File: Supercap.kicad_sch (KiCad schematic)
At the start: 0 parts

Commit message: began setup of hierarchial boards for supercap
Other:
- added sheet Control (Control/control.kicad_sch)
- added sheet Housekeeping (Housekeeping/housekeeping.kicad_sch)
- added sheet Supercap (Supercap/supercap.kicad_sch)
- added sheet Voltage Converter (Converter/converter.kicad_sch)
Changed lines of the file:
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@@
 	(generator_version "9.0")
 	(paper "A4")
+	(sheet
+		(at 109.22 68.58)
+		(size 41.91 25.4)
+		(exclude_from_sim no)
+		(in_bom yes)
+		(on_board yes)
+		(dnp no)
+		(fields_autoplaced yes)
+		(stroke
+			(width 0.1524)
+			(type solid)
+		)
+		(fill
+			(color 0 0 0 0.0000)
+		)
+		(property "Sheetname" "Housekeeping"
+			(at 109.22 67.8684 0)
+			(effects
+				(font
+					(size 1.27 1.27)
+				)
+				(justify left bottom)
+			)
+		)
+		(property "Sheetfile" "Housekeeping/housekeeping.kicad_sch"
+			(at 109.22 94.5646 0)
+			(effects
+				(font
+					(size 1.27 1.27)
+				)
+				(justify left top)
+			)
+		)
+		(instances
+			(project "Supercap"
+				(path "/98ee8313-37ab-4329-91ab-b5710476f82f"
+					(page "3")
+				)
+			)
+		)
+	)
+	(sheet
+		(at 158.75 68.58)
+		(size 39.37 25.4)
+		(exclude_from_sim no)
+		(in_bom yes)
+		(on_board yes)
+		(dnp no)
+		(fields_autoplaced yes)
+		(stroke
+			(width 0.1524)
+			(type solid)
+		)
+		(fill
+			(color 0 0 0 0.0000)
+		)
+		(property "Sheetname" "Voltage Converter"
+			(at 158.75 67.8684 0)
+			(effects
+				(font
+					(size 1.27 1.27)
+				)
+				(justify left bottom)
+			)
+		)
+		(property "Sheetfile" "Converter/converter.kicad_sch"
+			(at 158.75 94.5646 0)
+			(effects
+				(font
+					(size 1.27 1.27)
+				)
+				(justify left top)
+			)
+		)
+		(instances
+			(project "Supercap"
+				(path "/98ee8313-37ab-4329-91ab-b5710476f82f"
+					(page "4")
+				)
+			)
+		)
+	)
+	(sheet
+		(at 208.28 68.58)
+		(size 40.64 25.4)
+		(exclude_from_sim no)
+		(in_bom yes)
+		(on_board yes)
+		(dnp no)
+		(fields_autoplaced yes)
+		(stroke
+			(width 0.1524)
+			(type solid)
+		)
+		(fill
+			(color 0 0 0 0.0000)
+		)
+		(property "Sheetname" "Supercap"
+			(at 208.28 67.8684 0)
+			(effects
+				(font
+					(size 1.27 1.27)
+				)
+				(justify left bottom)
+			)
+		)
+		(property "Sheetfile" "Supercap/supercap.kicad_sch"
+			(at 208.28 94.5646 0)
+			(effects
+				(font
+					(size 1.27 1.27)
+				)
+				(justify left top)
+			)
+		)
+		(instances
+			(project "Supercap"
+				(path "/98ee8313-37ab-4329-91ab-b5710476f82f"
+					(page "5")
+				)
+			)
+		)
+	)
+	(sheet
+		(at 54.61 67.31)
+		(size 44.45 26.67)
+		(exclude_from_sim no)
+		(in_bom yes)
+		(on_board yes)
+		(dnp no)
+		(fields_autoplaced yes)
+		(stroke
+			(width 0.1524)
+			(type solid)
+		)
+		(fill
+			(color 0 0 0 0.0000)
+		)
+		(property "Sheetname" "Control"
+			(at 54.61 66.5984 0)
+			(effects
+				(font
+					(size 1.27 1.27)
+				)
+				(justify left bottom)
+			)
+		)
+		(property "Sheetfile" "Control/control.kicad_sch"
+			(at 54.61 94.5646 0)
+			(effects
+				(font
+					(size 1.27 1.27)
+				)
+				(justify left top)
+			)
+		)
+		(instances
+			(project "Supercap"
+				(path "/98ee8313-37ab-4329-91ab-b5710476f82f"
+					(page "2")
+				)
+			)
+		)
+	)
 	(sheet_instances
 		(path "/"

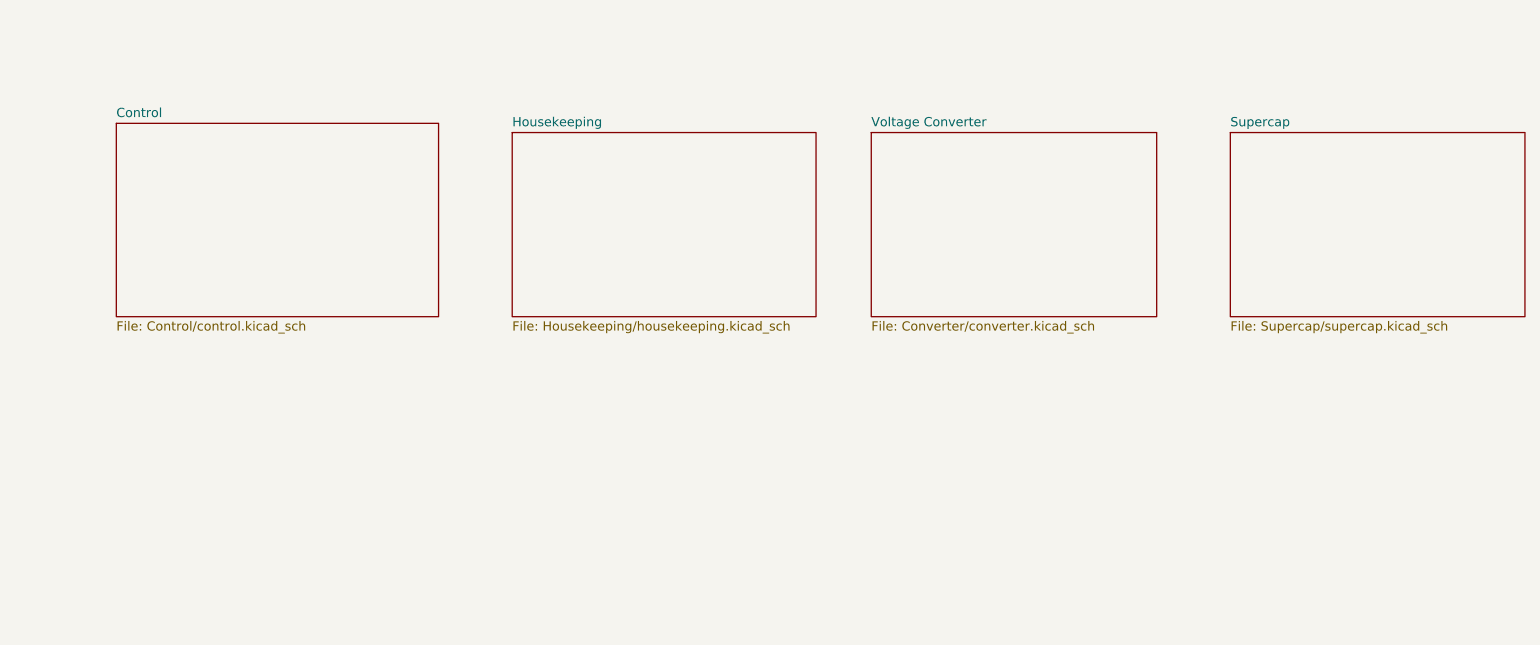
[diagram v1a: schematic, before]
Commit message: added more flesh to overall structure, primarily on converter stage
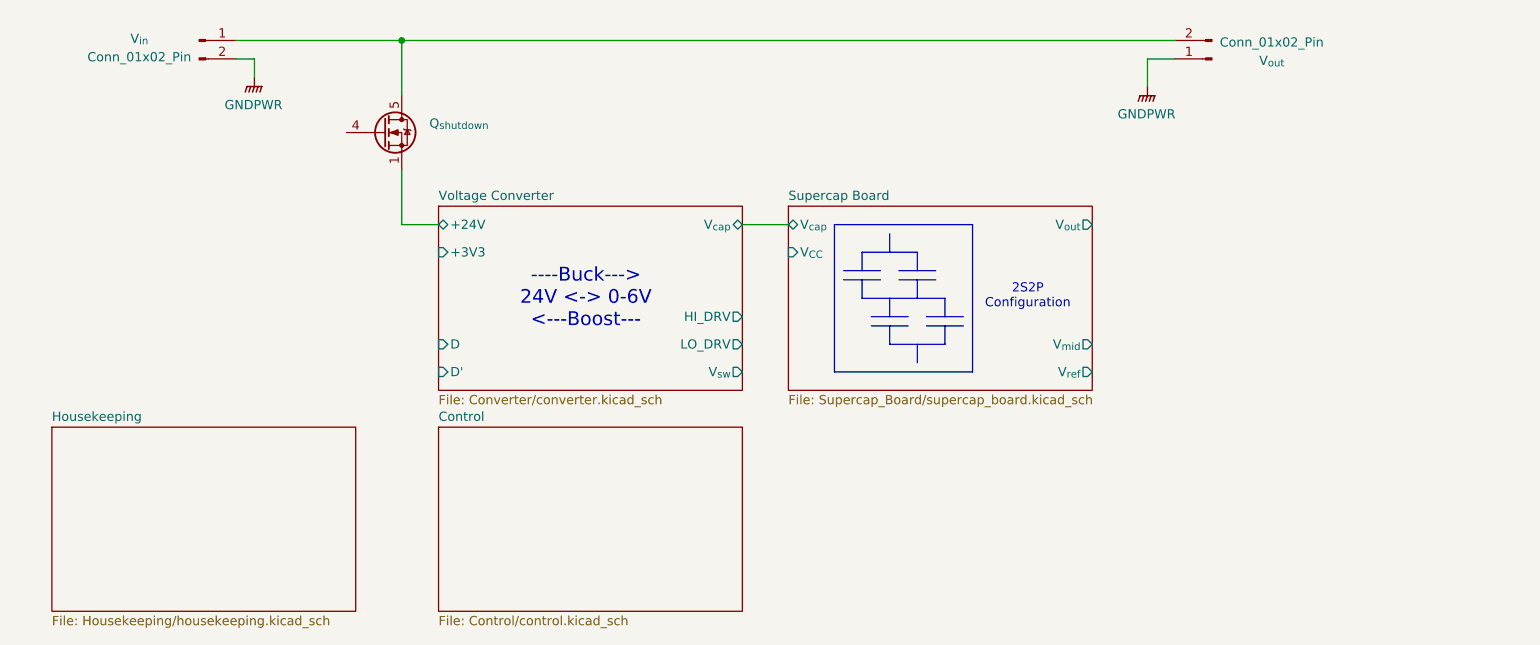
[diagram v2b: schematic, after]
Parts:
- added Q_{shutdown}: (no value), symbol Transistor_FET:FDMS8350LET40
- added V_{in}, V_{out}: Conn_01x02_Pin, symbol Connector:Conn_01x02_Pin
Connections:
- new net: Q_{shutdown}.5 (D), V_{in}.1 (Pin_1), V_{out}.2 (Pin_2)
- new net GNDPWR: V_{in}.2 (Pin_2), V_{out}.1 (Pin_1)
- new net Voltage Converter/+24V: Q_{shutdown}.1 (S), Q_{shutdown}.2 (S), Q_{shutdown}.3 (S)
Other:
- sheet Supercap renamed Supercap Board
- sheet Supercap Board: file Supercap/supercap.kicad_sch -> Supercap_Board/supercap_board.kicad_sch
- sheet Supercap Board ports: added V_{CC}, V_{cap}, V_{mid}, V_{out}, V_{ref}; removed none
- sheet Voltage Converter ports: added +24V, +3V3, D, D', HI_DRV, LO_DRV, V_{cap}, V_{sw}; removed none
- note added: "----Buck---> 24V <-> 0-6V <---Boost---"
- note added: "2S2P Configuration"

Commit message: finished first pass of general block diagram
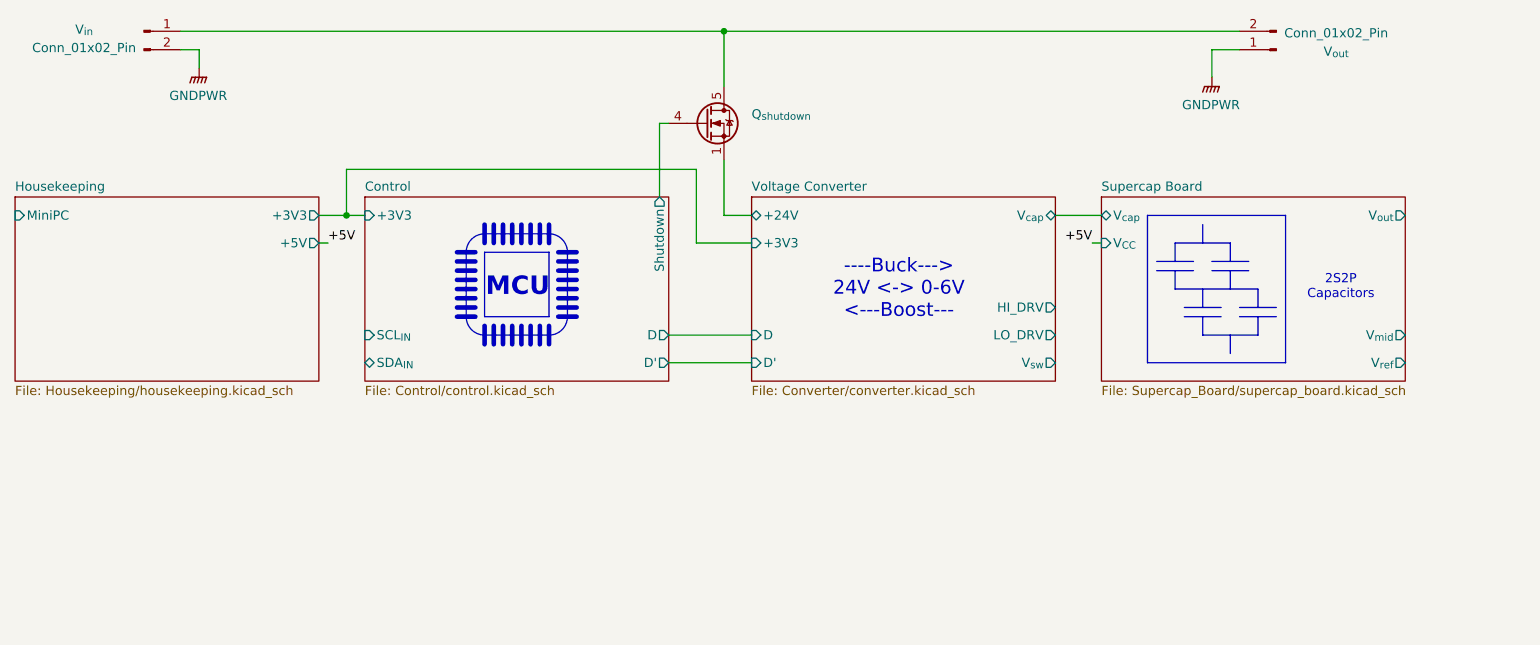
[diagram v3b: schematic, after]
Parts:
- Q_{shutdown}: value (none) -> ~
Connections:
- net Control/Shutdown: now reaches Q_{shutdown}.4 (G)
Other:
- sheet Control ports: added +3V3, D, D', SCL_{IN}, SDA_{IN}, Shutdown; removed none
- sheet Housekeeping ports: added +3V3, +5V, MiniPC; removed none
- note added: "2S2P Capacitors"
- note added: "MCU"
- note removed: "2S2P Configuration"
- moved on the sheet: Q_{shutdown}, V_{in}, V_{out}

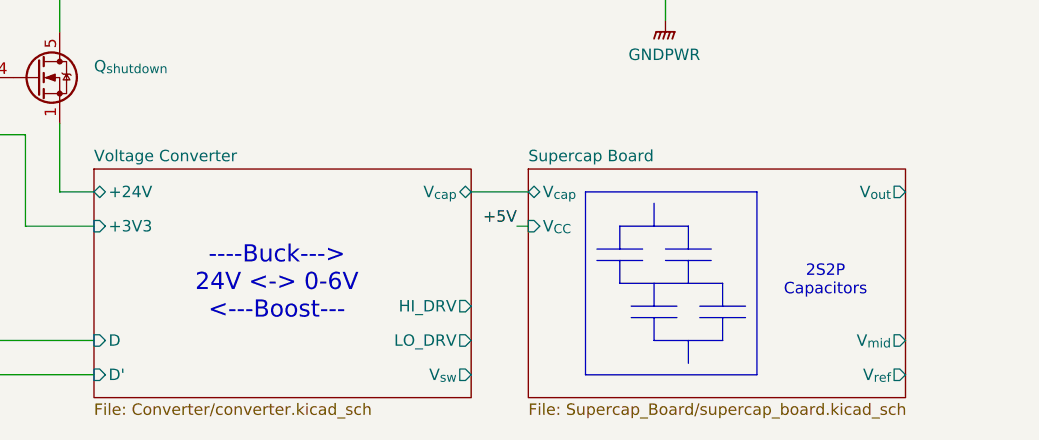
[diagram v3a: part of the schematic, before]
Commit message: replaced 2p2s caps with full parallel
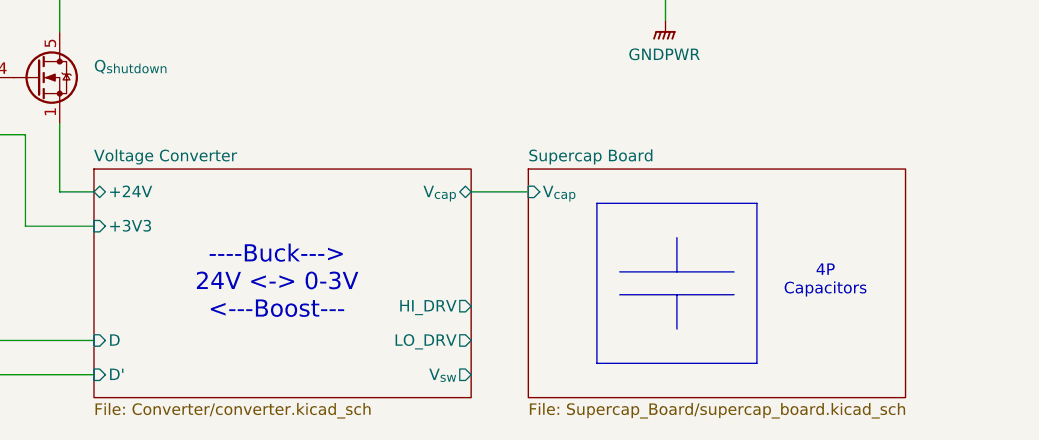
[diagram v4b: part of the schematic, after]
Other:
- sheet Supercap Board ports: added none; removed V_{CC}, V_{mid}, V_{out}, V_{ref}
- note added: "----Buck---> 24V <-> 0-3V <---Boost---"
- note added: "4P Capacitors"
- note removed: "----Buck---> 24V <-> 0-6V <---Boost---"
- note removed: "2S2P Capacitors"
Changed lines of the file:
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@@
 	)
 	(rectangle
-		(start 196.85 80.01)
-		(end 215.9 100.33)
+		(start 198.12 81.28)
+		(end 215.9 99.06)
 		(stroke
 			(width 0)
@@
 		)
 	)
-	(text "----Buck--->\n24V <-> 0-6V\n<---Boost---"
+	(text "----Buck--->\n24V <-> 0-3V\n<---Boost---"
 		(exclude_from_sim no)
 		(at 162.56 90.17 0)
@@
 		)
 	)
-	(text "2S2P\nCapacitors"
+	(text "4P\nCapacitors"
 		(exclude_from_sim no)
 		(at 223.52 89.916 0)
@@
 	(polyline
 		(pts
-			(xy 208.28 87.63) (xy 208.28 90.17)
+			(xy 207.01 91.44) (xy 207.01 95.25)
 		)
 		(stroke
@@
 	(wire
 		(pts
-			(xy 189.23 83.82) (xy 190.5 83.82)
-		)
-		(stroke
-			(width 0)
-			(type default)
-		)
-	)
-	(wire
-		(pts
 			(xy 184.15 80.01) (xy 190.5 80.01)
 		)
@@
 	(polyline
 		(pts
-			(xy 205.74 86.36) (xy 210.82 86.36)
-		)
-		(stroke
-			(width 0)
-			(type default)
-		)
-	)
-	(polyline
-		(pts
 			(xy 106.68 83.82) (xy 106.68 81.28)
 		)
@@
 		)
 	)
-	(polyline
-		(pts
-			(xy 200.66 83.82) (xy 200.66 86.36)
-		)
-		(stroke
-			(width 0)
-			(type default)
-		)
-	)
 	(wire
 		(pts
@@
 	(polyline
 		(pts
-			(xy 204.47 90.17) (xy 204.47 92.71)
+			(xy 200.66 91.44) (xy 213.36 91.44)
 		)
 		(stroke
@@
 	(polyline
 		(pts
-			(xy 204.47 96.52) (xy 212.09 96.52)
-		)
-		(stroke
-			(width 0)
-			(type default)
-		)
-	)
-	(polyline
-		(pts
 			(xy 115.57 91.44) (xy 118.11 91.44)
 		)
@@
 	(polyline
 		(pts
-			(xy 208.28 83.82) (xy 208.28 86.36)
-		)
-		(stroke
-			(width 0)
-			(type default)
-		)
-	)
-	(polyline
-		(pts
-			(xy 201.93 92.71) (xy 207.01 92.71)
-		)
-		(stroke
-			(width 0)
-			(type default)
-		)
-	)
-	(polyline
-		(pts
 			(xy 115.57 86.36) (xy 118.11 86.36)
 		)
@@
 	(polyline
 		(pts
-			(xy 201.93 93.98) (xy 207.01 93.98)
-		)
-		(stroke
-			(width 0)
-			(type default)
-		)
-	)
-	(polyline
-		(pts
-			(xy 212.09 93.98) (xy 212.09 96.52)
-		)
-		(stroke
-			(width 0)
-			(type default)
-		)
-	)
-	(polyline
-		(pts
 			(xy 115.57 87.63) (xy 118.11 87.63)
 		)
@@
 	(polyline
 		(pts
-			(xy 205.74 87.63) (xy 210.82 87.63)
-		)
-		(stroke
-			(width 0)
-			(type default)
-		)
-	)
-	(polyline
-		(pts
 			(xy 111.76 83.82) (xy 111.76 81.28)
 		)
@@
 	(polyline
 		(pts
+			(xy 200.66 88.9) (xy 213.36 88.9)
+		)
+		(stroke
+			(width 0)
+			(type default)
+		)
+	)
+	(polyline
+		(pts
 			(xy 101.6 90.17) (xy 104.14 90.17)
 		)
@@
 	(polyline
 		(pts
+			(xy 207.01 85.09) (xy 207.01 88.9)
+		)
+		(stroke
+			(width 0)
+			(type default)
+		)
+	)
+	(polyline
+		(pts
 			(xy 101.6 91.44) (xy 104.14 91.44)
 		)
@@
 	(polyline
 		(pts
-			(xy 204.47 93.98) (xy 204.47 96.52)
-		)
-		(stroke
-			(width 0)
-			(type default)
-		)
-	)
-	(polyline
-		(pts
 			(xy 116.84 85.09) (xy 116.84 93.98)
 		)
@@
 		)
 	)
-	(polyline
-		(pts
-			(xy 209.55 92.71) (xy 214.63 92.71)
-		)
-		(stroke
-			(width 0)
-			(type default)
-		)
-	)
 	(wire
 		(pts
@@
 	(polyline
 		(pts
-			(xy 200.66 90.17) (xy 212.09 90.17)
-		)
-		(stroke
-			(width 0)
-			(type default)
-		)
-	)
-	(polyline
-		(pts
 			(xy 101.6 88.9) (xy 104.14 88.9)
 		)
@@
 	(polyline
 		(pts
-			(xy 209.55 93.98) (xy 214.63 93.98)
-		)
-		(stroke
-			(width 0)
-			(type default)
-		)
-	)
-	(polyline
-		(pts
-			(xy 198.12 87.63) (xy 203.2 87.63)
-		)
-		(stroke
-			(width 0)
-			(type default)
-		)
-	)
-	(polyline
-		(pts
-			(xy 200.66 83.82) (xy 208.28 83.82)
-		)
-		(stroke
-			(width 0)
-			(type default)
-		)
-	)
-	(polyline
-		(pts
 			(xy 115.57 93.98) (xy 118.11 93.98)
 		)
@@
 	(polyline
 		(pts
-			(xy 198.12 86.36) (xy 203.2 86.36)
-		)
-		(stroke
-			(width 0)
-			(type default)
-		)
-	)
-	(polyline
-		(pts
 			(xy 109.22 83.82) (xy 109.22 81.28)
 		)
@@
 	(polyline
 		(pts
-			(xy 204.47 81.28) (xy 204.47 83.82)
-		)
-		(stroke
-			(width 0)
-			(type default)
-		)
-	)
-	(polyline
-		(pts
 			(xy 114.3 97.79) (xy 114.3 95.25)
 		)
@@
 		)
 	)
-	(polyline
-		(pts
-			(xy 212.09 90.17) (xy 212.09 92.71)
-		)
-		(stroke
-			(width 0)
-			(type default)
-		)
-	)
 	(wire
 		(pts
@@
 		)
 	)
-	(polyline
-		(pts
-			(xy 208.28 96.52) (xy 208.28 99.06)
-		)
-		(stroke
-			(width 0)
-			(type default)
-		)
-	)
 	(wire
 		(pts
@@
 		)
 	)
-	(polyline
-		(pts
-			(xy 200.66 87.63) (xy 200.66 90.17)
-		)
-		(stroke
-			(width 0)
-			(type default)
-		)
-	)
 	(wire
 		(pts
@@
 			(width 0)
 			(type default)
-		)
-	)
-	(label "+5V"
-		(at 189.23 83.82 180)
-		(effects
-			(font
-				(size 1.27 1.27)
-			)
-			(justify right bottom)
 		)
 	)
@@
 			)
 		)
-		(pin "V_{out}" output
-			(at 232.41 80.01 0)
-			(effects
-				(font
-					(size 1.27 1.27)
-				)
-				(justify right)
-			)
-		)
-		(pin "V_{cap}" bidirectional
+		(pin "V_{cap}" input
 			(at 190.5 80.01 180)
 			(effects
@@
 			)
 		)
-		(pin "V_{CC}" input
-			(at 190.5 83.82 180)
-			(effects
-				(font
-					(size 1.27 1.27)
-				)
-				(justify left)
-			)
-		)
-		(pin "V_{mid}" output
-			(at 232.41 96.52 0)
-			(effects
-				(font
-					(size 1.27 1.27)
-				)
-				(justify right)
-			)
-		)
-		(pin "V_{ref}" output
-			(at 232.41 100.33 0)
-			(effects
-				(font
-					(size 1.27 1.27)
-				)
-				(justify right)
-			)
-		)

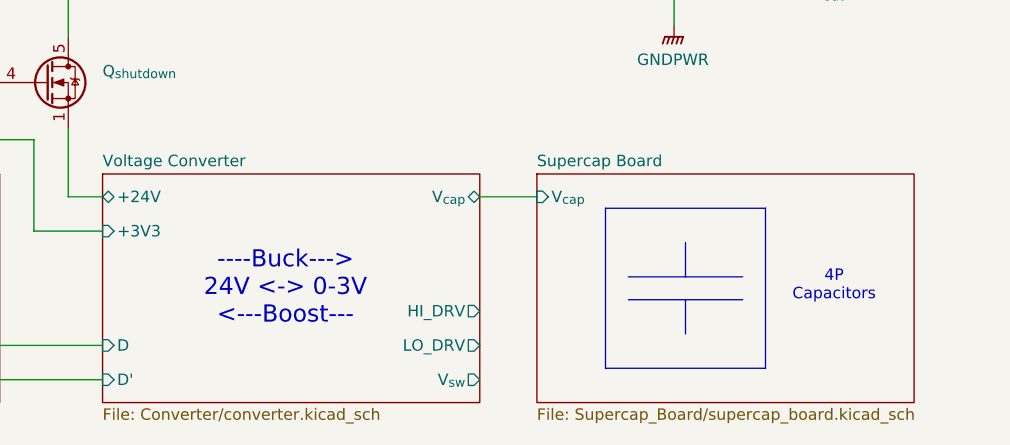
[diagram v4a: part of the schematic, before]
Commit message: switched capacitor topology to 4S
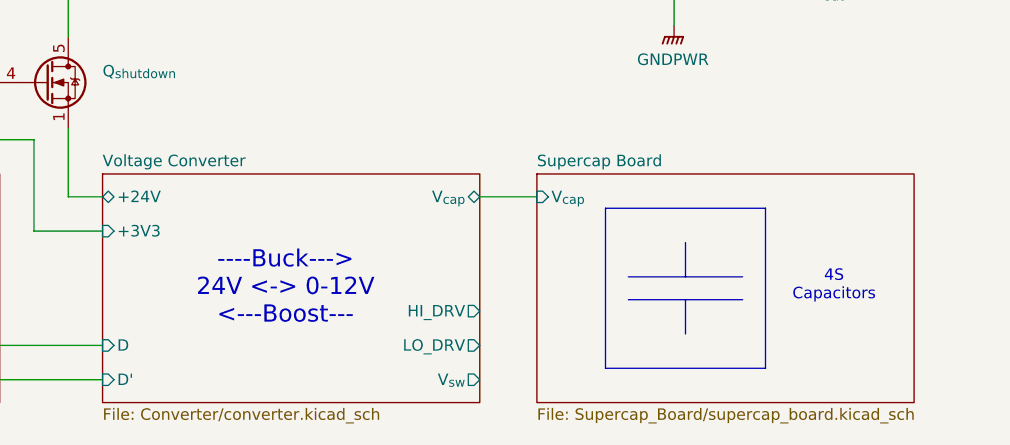
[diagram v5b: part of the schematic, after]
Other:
- note added: "----Buck---> 24V <-> 0-12V <---Boost---"
- note added: "4S Capacitors"
- note removed: "----Buck---> 24V <-> 0-3V <---Boost---"
- note removed: "4P Capacitors"
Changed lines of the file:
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@@
 		)
 	)
-	(text "----Buck--->\n24V <-> 0-3V\n<---Boost---"
+	(text "----Buck--->\n24V <-> 0-12V\n<---Boost---"
 		(exclude_from_sim no)
 		(at 162.56 90.17 0)
@@
 		)
 	)
-	(text "4P\nCapacitors"
+	(text "4S\nCapacitors"
 		(exclude_from_sim no)
 		(at 223.52 89.916 0)
